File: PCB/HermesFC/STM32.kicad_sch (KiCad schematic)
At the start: 52 parts, among them J1 Conn_01x04, J2 Screw_Terminal_01x02, J3 Conn_01x04, J4 Conn_01x04, J5 Conn_01x04, J6 Conn_01x06, J7 USB_B_Micro, Q1 AO3401A, U1 STM32F405RGTx, U2 AP63203WU, U3 USBLC6-2SC6, Y1 16Mhz

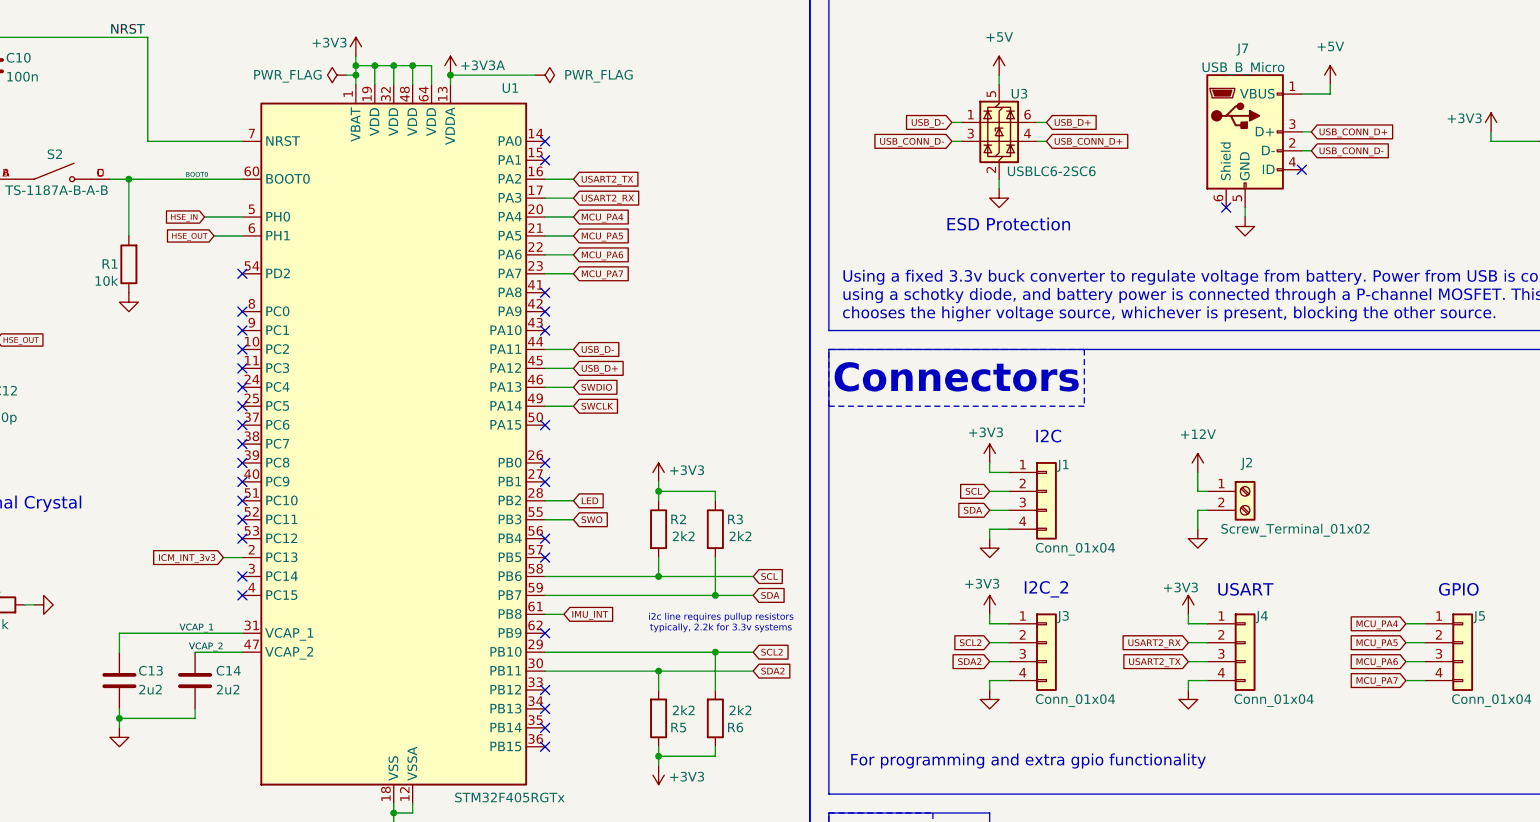
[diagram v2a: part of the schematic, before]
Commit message: update design to be more compact
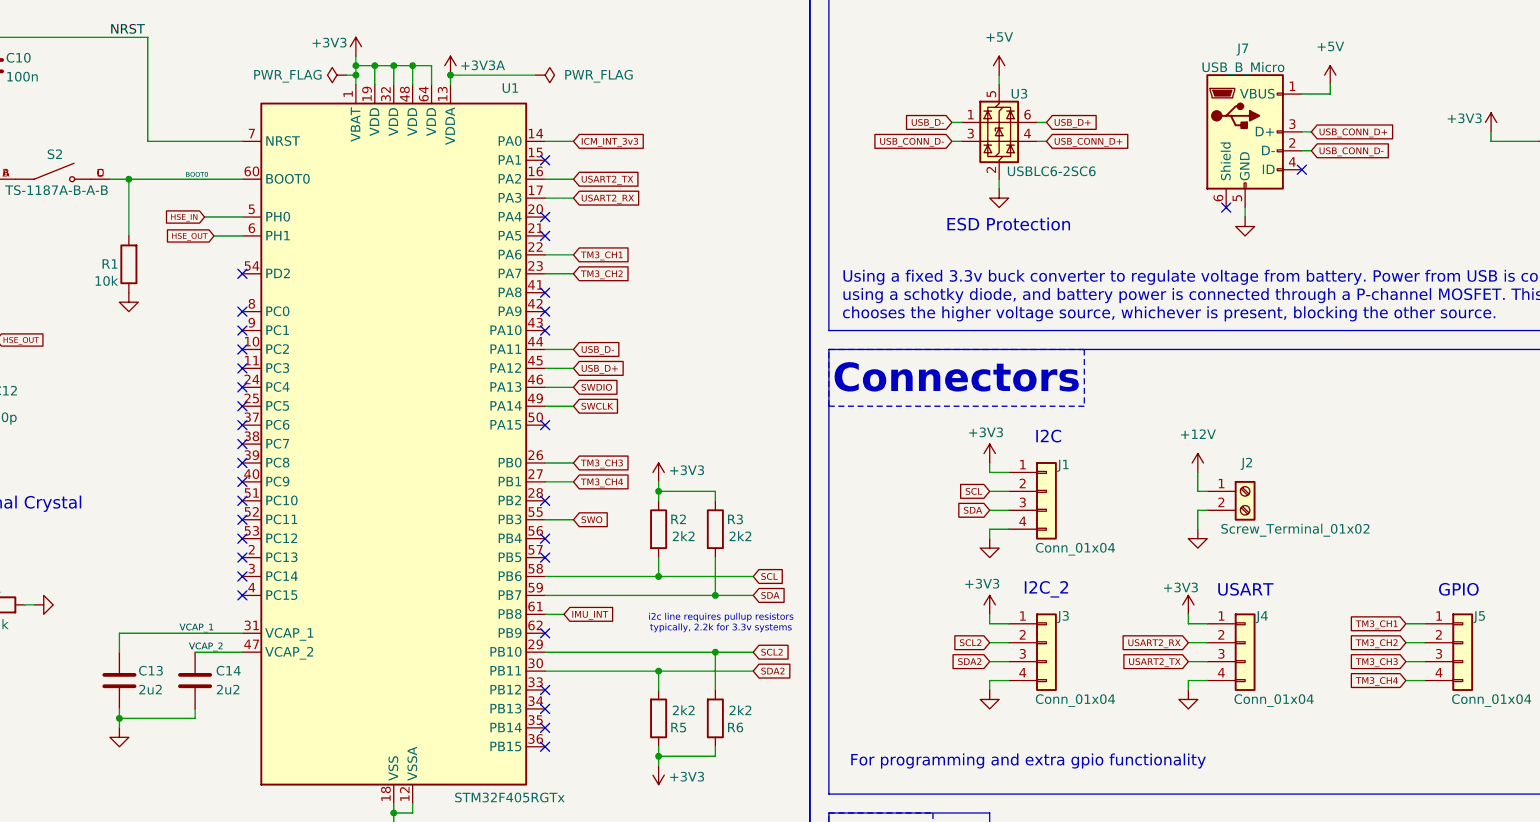
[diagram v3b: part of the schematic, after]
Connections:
- net ICM_INT_3v3: now also U1.14 (PA0); no longer U1.2 (PC13)
- net LED: no longer U1.28 (PB2)
- net TM3_CH3: now reaches U1.26 (PB0)
- net TM3_CH3: now also J5.3 (Pin_3)
- net TM3_CH4: now reaches U1.27 (PB1)
- net TM3_CH4: now also J5.4 (Pin_4)
- net MCU_PA4: no longer names the net of U1.20 (PA4)
- net MCU_PA4: no longer J5.1 (Pin_1)
- net MCU_PA5: no longer names the net of U1.21 (PA5)
- net MCU_PA5: no longer J5.2 (Pin_2)
- net MCU_PA6 renamed TM3_CH1
- net TM3_CH1: now also J5.1 (Pin_1); no longer J5.3 (Pin_3)
- net MCU_PA7 renamed TM3_CH2
- net TM3_CH2: now also J5.2 (Pin_2); no longer J5.4 (Pin_4)
- no-connect marks 33 -> 34
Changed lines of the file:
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@@
 	)
 	(no_connect
-		(at 115.57 120.65)
-	)
-	(no_connect
 		(at 74.93 95.25)
 	)
@@
 	)
 	(no_connect
+		(at 115.57 90.17)
+	)
+	(no_connect
 		(at 74.93 113.03)
 	)
@@
 	)
 	(no_connect
-		(at 115.57 123.19)
-	)
-	(no_connect
 		(at 74.93 110.49)
 	)
@@
 	)
 	(no_connect
+		(at 115.57 87.63)
+	)
+	(no_connect
 		(at 207.01 86.36)
 	)
@@
 	)
 	(no_connect
+		(at 115.57 125.73)
+	)
+	(no_connect
 		(at 74.93 125.73)
 	)
@@
 	)
 	(no_connect
+		(at 74.93 133.35)
+	)
+	(no_connect
 		(at 115.57 143.51)
 	)
@@
 	)
 	(no_connect
-		(at 115.57 77.47)
-	)
-	(no_connect
 		(at 115.57 153.67)
 	)
@@
 	(wire
 		(pts
+			(xy 119.38 77.47) (xy 115.57 77.47)
+		)
+		(stroke
+			(width 0)
+			(type default)
+		)
+	)
+	(wire
+		(pts
 			(xy 71.12 90.17) (xy 74.93 90.17)
 		)
@@
 	(wire
 		(pts
-			(xy 72.39 133.35) (xy 74.93 133.35)
-		)
-		(stroke
-			(width 0)
-			(type default)
-		)
-	)
-	(wire
-		(pts
 			(xy 242.57 76.2) (xy 242.57 77.47)
 		)
@@
 	(wire
 		(pts
-			(xy 115.57 125.73) (xy 119.38 125.73)
-		)
-		(stroke
-			(width 0)
-			(type default)
-		)
-	)
-	(wire
-		(pts
 			(xy 62.23 63.5) (xy 62.23 77.47)
 		)
@@
 	(wire
 		(pts
+			(xy 115.57 123.19) (xy 119.38 123.19)
+		)
+		(stroke
+			(width 0)
+			(type default)
+		)
+	)
+	(wire
+		(pts
 			(xy 203.2 124.46) (xy 204.47 124.46)
 		)
@@
 	(wire
 		(pts
-			(xy 115.57 90.17) (xy 119.38 90.17)
-		)
-		(stroke
-			(width 0)
-			(type default)
-		)
-	)
-	(wire
-		(pts
-			(xy 115.57 87.63) (xy 119.38 87.63)
-		)
-		(stroke
-			(width 0)
-			(type default)
-		)
-	)
-	(wire
-		(pts
 			(xy 217.17 78.74) (xy 218.44 78.74)
 		)
@@
 	(wire
 		(pts
+			(xy 115.57 120.65) (xy 119.38 120.65)
+		)
+		(stroke
+			(width 0)
+			(type default)
+		)
+	)
+	(wire
+		(pts
 			(xy 274.32 30.48) (xy 274.32 33.02)
 		)
@@
 		)
 	)
-	(global_label "MCU_PA6"
-		(shape input)
-		(at 231.14 147.32 180)
-		(fields_autoplaced yes)
-		(effects
-			(font
-				(size 0.889 0.889)
-			)
-			(justify right)
-		)
-		(property "Intersheetrefs" "${INTERSHEET_REFS}"
-			(at 223.0392 147.32 0)
-			(effects
-				(font
-					(size 1.27 1.27)
-				)
-				(justify right)
-				(hide yes)
-			)
-		)
-	)
 	(global_label "USART2_RX"
 		(shape input)
@@
 		)
 	)
-	(global_label "ICM_INT_3v3"
+	(global_label "TM3_CH2"
 		(shape input)
-		(at 72.39 133.35 180)
-		(fields_autoplaced yes)
-		(effects
-			(font
-				(size 0.889 0.889)
-			)
-			(justify right)
-		)
-		(property "Intersheetrefs" "${INTERSHEET_REFS}"
-			(at 62.215 133.35 0)
-			(effects
-				(font
-					(size 1.27 1.27)
-				)
-				(justify right)
-				(hide yes)
-			)
-		)
-	)
-	(global_label "MCU_PA4"
-		(shape input)
-		(at 231.14 142.24 180)
+		(at 231.14 144.78 180)
 		(fields_autoplaced yes)
 		(effects
@@
 		)
 		(property "Intersheetrefs" "${INTERSHEET_REFS}"
-			(at 223.0392 142.24 0)
+			(at 223.1662 144.78 0)
 			(effects
 				(font
@@
 		)
 	)
-	(global_label "MCU_PA7"
-		(shape input)
-		(at 231.14 149.86 180)
-		(fields_autoplaced yes)
-		(effects
-			(font
-				(size 0.889 0.889)
-			)
-			(justify right)
-		)
-		(property "Intersheetrefs" "${INTERSHEET_REFS}"
-			(at 223.0392 149.86 0)
-			(effects
-				(font
-					(size 1.27 1.27)
-				)
-				(justify right)
-				(hide yes)
-			)
-		)
-	)
 	(global_label "USB_CONN_D-"
 		(shape input)
@@
 		)
 	)
-	(global_label "LED"
-		(shape input)
-		(at 119.38 125.73 0)
-		(fields_autoplaced yes)
-		(effects
-			(font
-				(size 0.889 0.889)
-			)
-			(justify left)
-		)
-		(property "Intersheetrefs" "${INTERSHEET_REFS}"
-			(at 123.8825 125.73 0)
-			(effects
-				(font
-					(size 1.27 1.27)
-				)
-				(justify left)
-				(hide yes)
-			)
-		)
-	)
 	(global_label "SCL2"
 		(shape input)
@@
 		)
 	)
-	(global_label "MCU_PA7"
+	(global_label "TM3_CH2"
 		(shape input)
 		(at 119.38 95.25 0)
@@
 		)
 		(property "Intersheetrefs" "${INTERSHEET_REFS}"
-			(at 127.4808 95.25 0)
+			(at 127.3538 95.25 0)
 			(effects
 				(font
@@
 		)
 	)
-	(global_label "MCU_PA4"
+	(global_label "TM3_CH3"
 		(shape input)
-		(at 119.38 87.63 0)
+		(at 119.38 120.65 0)
 		(fields_autoplaced yes)
 		(effects
@@
 		)
 		(property "Intersheetrefs" "${INTERSHEET_REFS}"
-			(at 127.4808 87.63 0)
+			(at 127.3538 120.65 0)
 			(effects
 				(font
@@
 		)
 	)
+	(global_label "TM3_CH4"
+		(shape input)
+		(at 231.14 149.86 180)
+		(fields_autoplaced yes)
+		(effects
+			(font
+				(size 0.889 0.889)
+			)
+			(justify right)
+		)
+		(property "Intersheetrefs" "${INTERSHEET_REFS}"
+			(at 223.1662 149.86 0)
+			(effects
+				(font
+					(size 1.27 1.27)
+				)
+				(justify right)
+				(hide yes)
+			)
+		)
+	)
 	(global_label "IMU_INT"
 		(shape input)
@@
 		)
 	)
+	(global_label "TM3_CH1"
+		(shape input)
+		(at 231.14 142.24 180)
+		(fields_autoplaced yes)
+		(effects
+			(font
+				(size 0.889 0.889)
+			)
+			(justify right)
+		)
+		(property "Intersheetrefs" "${INTERSHEET_REFS}"
+			(at 223.1662 142.24 0)
+			(effects
+				(font
+					(size 1.27 1.27)
+				)
+				(justify right)
+				(hide yes)
+			)
+		)
+	)
 	(global_label "SWDIO"
 		(shape input)
@@
 		)
 	)
+	(global_label "ICM_INT_3v3"
+		(shape input)
+		(at 119.38 77.47 0)
+		(fields_autoplaced yes)
+		(effects
+			(font
+				(size 0.889 0.889)
+			)
+			(justify left)
+		)
+		(property "Intersheetrefs" "${INTERSHEET_REFS}"
+			(at 129.555 77.47 0)
+			(effects
+				(font
+					(size 1.27 1.27)
+				)
+				(justify left)
+				(hide yes)
+			)
+		)
+	)
 	(global_label "SDA2"
 		(shape input)
@@
 		)
 	)
-	(global_label "MCU_PA5"
+	(global_label "TM3_CH3"
 		(shape input)
-		(at 231.14 144.78 180)
+		(at 231.14 147.32 180)
 		(fields_autoplaced yes)
 		(effects
@@
 		)
 		(property "Intersheetrefs" "${INTERSHEET_REFS}"
-			(at 223.0392 144.78 0)
+			(at 223.1662 147.32 0)
 			(effects
 				(font
@@
 		)
 	)
-	(global_label "MCU_PA5"
+	(global_label "TM3_CH4"
 		(shape input)
-		(at 119.38 90.17 0)
+		(at 119.38 123.19 0)
 		(fields_autoplaced yes)
 		(effects
@@
 		)
 		(property "Intersheetrefs" "${INTERSHEET_REFS}"
-			(at 127.4808 90.17 0)
+			(at 127.3538 123.19 0)
 			(effects
 				(font
@@
 		)
 	)
-	(global_label "MCU_PA6"
+	(global_label "TM3_CH1"
 		(shape input)
 		(at 119.38 92.71 0)
@@
 		)
 		(property "Intersheetrefs" "${INTERSHEET_REFS}"
-			(at 127.4808 92.71 0)
+			(at 127.3538 92.71 0)
 			(effects
 				(font

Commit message: complete compact routing
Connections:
- net LED: now also U1.51 (PC10)
- net SWCLK: now also J6.3 (Pin_3); no longer J6.2 (Pin_2)
- net SWDIO: now also J6.2 (Pin_2); no longer J6.3 (Pin_3)
- no-connect marks 34 -> 33
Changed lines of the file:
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@@
-	)
-	(no_connect
-		(at 74.93 125.73)
 	)
 	(no_connect
@@
 		(pts
 			(xy 210.82 52.07) (xy 228.6 52.07)
+		)
+		(stroke
+			(width 0)
+			(type default)
+		)
+	)
+	(wire
+		(pts
+			(xy 71.12 125.73) (xy 74.93 125.73)
 		)
 		(stroke
@@
 	(global_label "SWDIO"
 		(shape input)
-		(at 261.62 142.24 180)
+		(at 261.62 139.7 180)
 		(fields_autoplaced yes)
 		(effects
@@
 		)
 		(property "Intersheetrefs" "${INTERSHEET_REFS}"
-			(at 255.4242 142.24 0)
+			(at 255.4242 139.7 0)
 			(effects
 				(font
@@
 	(global_label "SWCLK"
 		(shape input)
-		(at 261.62 139.7 180)
+		(at 261.62 142.24 180)
 		(fields_autoplaced yes)
 		(effects
@@
 		)
 		(property "Intersheetrefs" "${INTERSHEET_REFS}"
-			(at 255.1701 139.7 0)
+			(at 255.1701 142.24 0)
 			(effects
 				(font
@@
 			(effects
 				(font
+					(size 1.27 1.27)
+				)
+				(justify right)
+				(hide yes)
+			)
+		)
+	)
+	(global_label "LED"
+		(shape input)
+		(at 71.12 125.73 180)
+		(fields_autoplaced yes)
+		(effects
+			(font
+				(size 0.889 0.889)
+			)
+			(justify right)
+		)
+		(property "Intersheetrefs" "${INTERSHEET_REFS}"
+			(at 66.6175 125.73 0)
+			(effects
+				(font

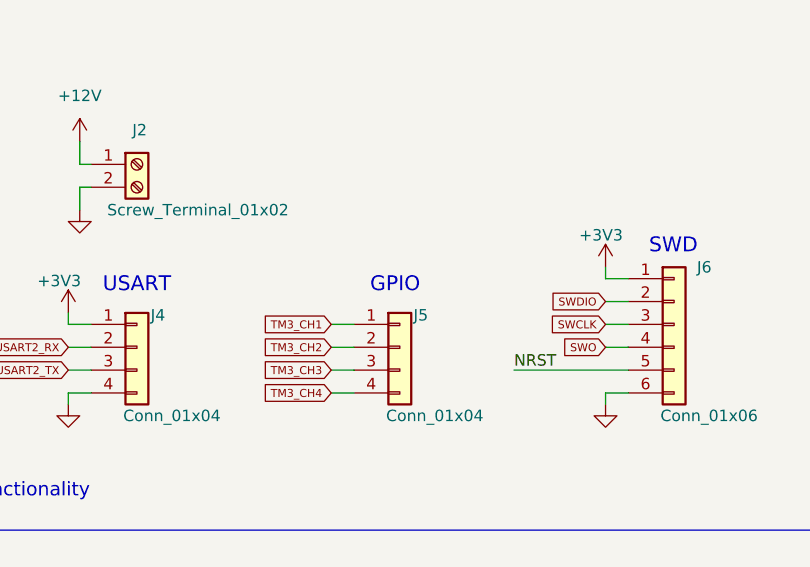
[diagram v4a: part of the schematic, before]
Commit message: new compact PCB design
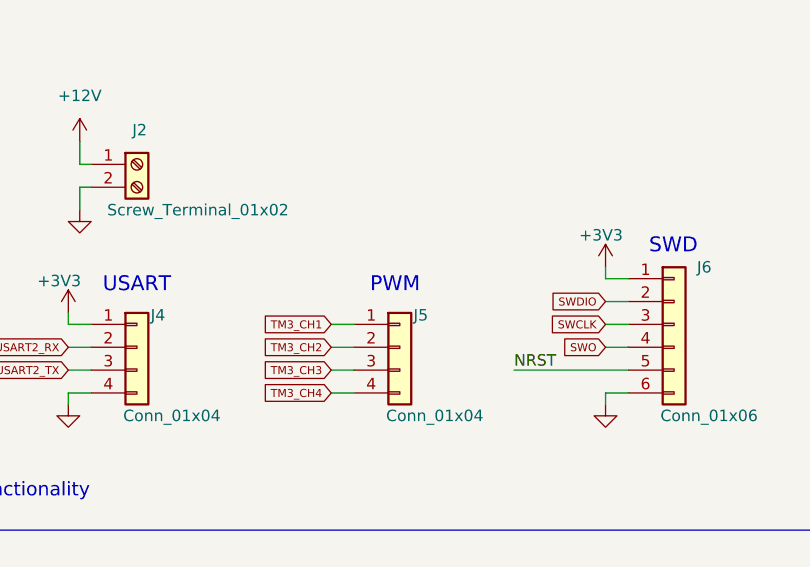
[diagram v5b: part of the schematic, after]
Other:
- note added: "PWM"
- note removed: "GPIO"
- title: MCU -> MCU + Power
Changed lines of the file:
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@@
 	(paper "A4")
 	(title_block
-		(title "MCU")
-		(date "2025-03-02")
-		(rev "v0.2")
+		(title "MCU + Power")
+		(date "2025-03-12")
+		(rev "v1.0")
 		(company "Aadil Naji")
+		(comment 1 "HERMES FLIGHT CONTROLLER")
 	)
 	(junction
@@
 		)
 	)
-	(text "GPIO"
+	(text "PWM"
 		(exclude_from_sim no)
 		(at 235.458 137.922 0)

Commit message: minor changes C18
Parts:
- C18: footprint Capacitor_SMD:C_0603_1608Metric -> Capacitor_SMD:C_0805_2012Metric
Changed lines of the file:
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@@
 			)
 		)
-		(property "Footprint" "Capacitor_SMD:C_0603_1608Metric"
+		(property "Footprint" "Capacitor_SMD:C_0805_2012Metric"
 			(at 246.0752 40.64 0)
 			(effects
